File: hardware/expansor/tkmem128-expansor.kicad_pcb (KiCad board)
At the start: 2 copper layers, 78.7 x 45 mm, 3 parts, among them J1 Terminais do conector, J2 Passagem

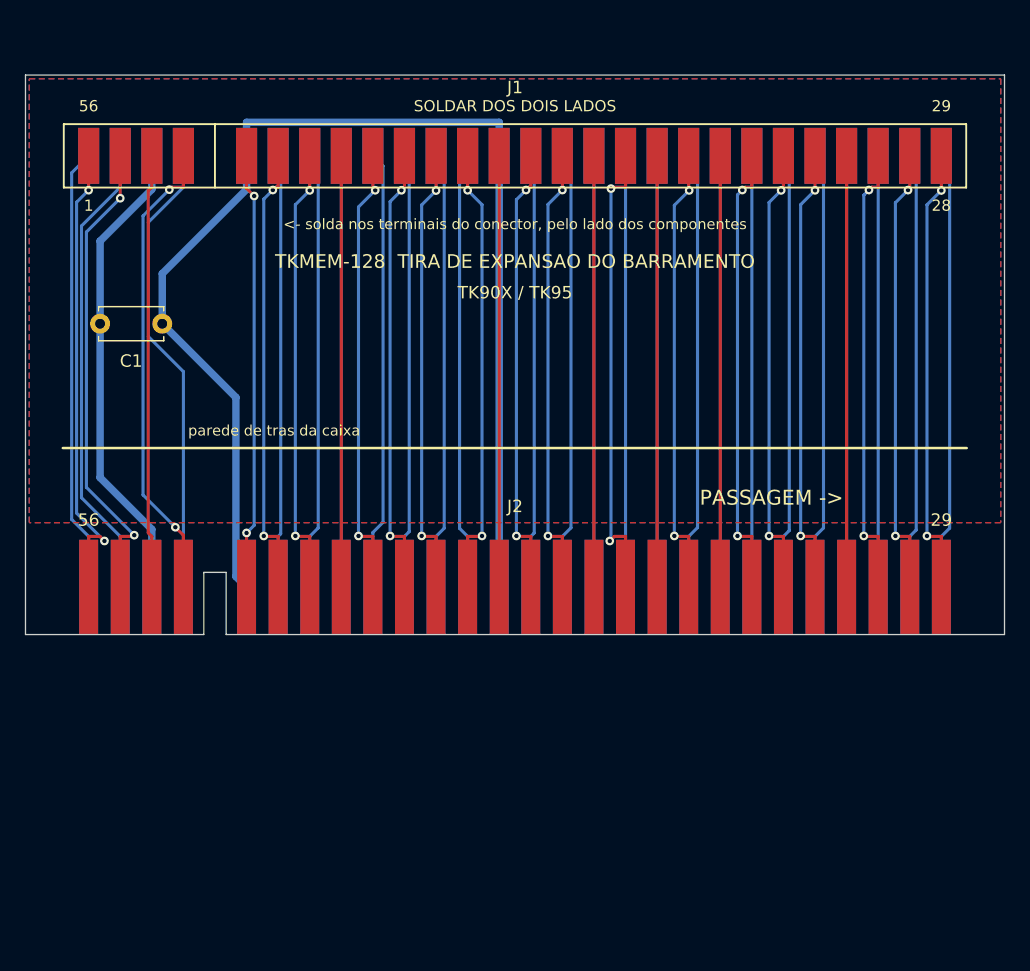
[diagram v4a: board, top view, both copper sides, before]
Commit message: Tira de expansao: ilhas de solda chegam ate a borda
As ilhas de J1 agora comecam na propria aresta da tira e entram 5 mm, em vez
de ficarem recuadas. Os terminais do TE 5645235 avancam 3,18 +-0,51 mm, mas ha
conectores com terminal mais curto - com a ilha na borda o terminal encontra
cobre em qualquer caso, e nao importa quanto a tira entra entre as fileiras.

Ajustes que vieram junto:

  mk_decoy.py  ganhou EDGE_PADS_TOP: a placa-isca nao pode recuar a aresta onde
               o cobre chega de proposito na borda, senao as ilhas ficariam
               fora do contorno e o roteador as trataria como obstaculo.
  .kicad_dru   regra de folga cobre-borda dispensada para J1, como ja havia
               para os dedos de J2.

Nota de fabricacao: o ENIG vale para a tira inteira, nao so para os dedos - as
ilhas de solda tambem chegam a borda.

Tira reroteada: ERC 0, DRC 0 erros, 0 desconexoes. Placa principal inalterada.

Co-Authored-By: Claude Opus 5 <noreply@anthropic.com>
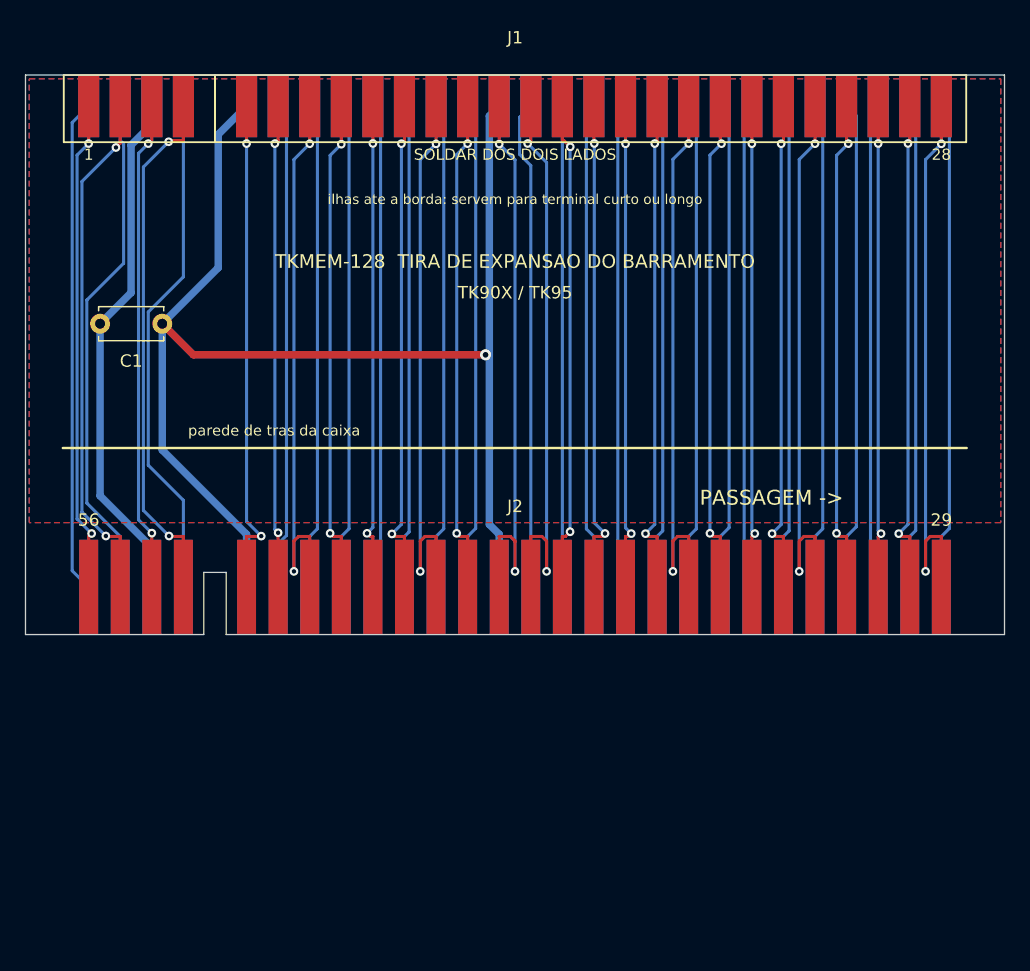
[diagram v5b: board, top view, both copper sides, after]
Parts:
- moved J1 4.00 mm to (39.4, 2.50)
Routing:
- net BUS_NMI: track 34.7 -> 45.9 mm, vias 0 -> 2
- net GND: track 100.7 -> 111.0 mm, vias 0 -> 1
- net BUS_HALT: track 36.3 -> 46.1 mm
- net BUS_P37: track 36.2 -> 45.9 mm
- net D2: track 36.2 -> 45.9 mm
- net BUS_P29: track 36.2 -> 45.9 mm
- net BUS_M1: track 36.2 -> 45.9 mm
- net D4: track 36.2 -> 45.9 mm
- net WR_N: track 34.7 -> 39.9 mm, vias 0 -> 2
- net D6: track 34.7 -> 39.8 mm, vias 0 -> 2
- net BUS_RFSH: track 34.7 -> 39.8 mm, vias 0 -> 2
- net D0: track 35.2 -> 40.3 mm
- net IORQ_N: track 34.7 -> 39.8 mm, vias 0 -> 2
- net BUS_WAIT: track 34.7 -> 39.7 mm, vias 0 -> 2
- net ROMCS_BUS: track 34.7 -> 39.3 mm
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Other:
- board text added: "ilhas ate a borda: servem para terminal curto ou longo"
- board text removed: "<- solda nos terminais do conector, pelo lado dos componentes"

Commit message: Tira estava espelhada em relacao a placa principal
A tira e soldada nos terminais do conector da principal, mas as colunas das
duas estavam invertidas ponta a ponta:

               coluna do pino 1     guia (coluna sem contato)
  principal    x = 73,66 mm         x = 63,50 mm
  tira         x =  5,08 mm         x = 15,24 mm     <- espelhado

Os dois layouts correm no MESMO sentido de X do mundo. Pela regra do KiCad
(Xl x Yl = -N para a face F.Cu vista de fora):

  principal: N = -Y (componentes para tras), Yl = -Z  =>  Xl = +X
  tira:      N = +Z (F.Cu para cima),        Yl = -Y  =>  Xl = +X

Logo a coluna de cada pino e a guia tem que cair no mesmo x nas duas placas.
Corrigido girando J1 e J2 da tira em 180 graus - como todas as ilhas dos dois
footprints estao em y local = 0, girar 180 espelha so o X e nao troca as faces.

Dois reforcos para isso nao voltar:

  gen_pcb.py  o rasgo da guia passa a ser DEDUZIDO do vao real entre as ilhas
              de J2, em vez de calculado pelo numero da coluna. Se o footprint
              girar, o rasgo acompanha.
  tools/confere_alinhamento.py  verificacao de regressao: confere colunas,
              guia, faces das fileiras e qual fileira fica junto a aresta,
              comparando as duas placas. Falha alto se algo desalinhar.

Esse era um erro que ERC e DRC nunca pegariam: cada projeto e valido
isoladamente, nada no KiCad amarra uma placa a outra. So apareceria na bancada,
com o barramento invertido. Documentado no item 5b de ANTES-DE-FABRICAR.

Tira reroteada: ERC 0, DRC 0 erros, 0 desconexoes. Principal inalterada.

Co-Authored-By: Claude Opus 5 <noreply@anthropic.com>
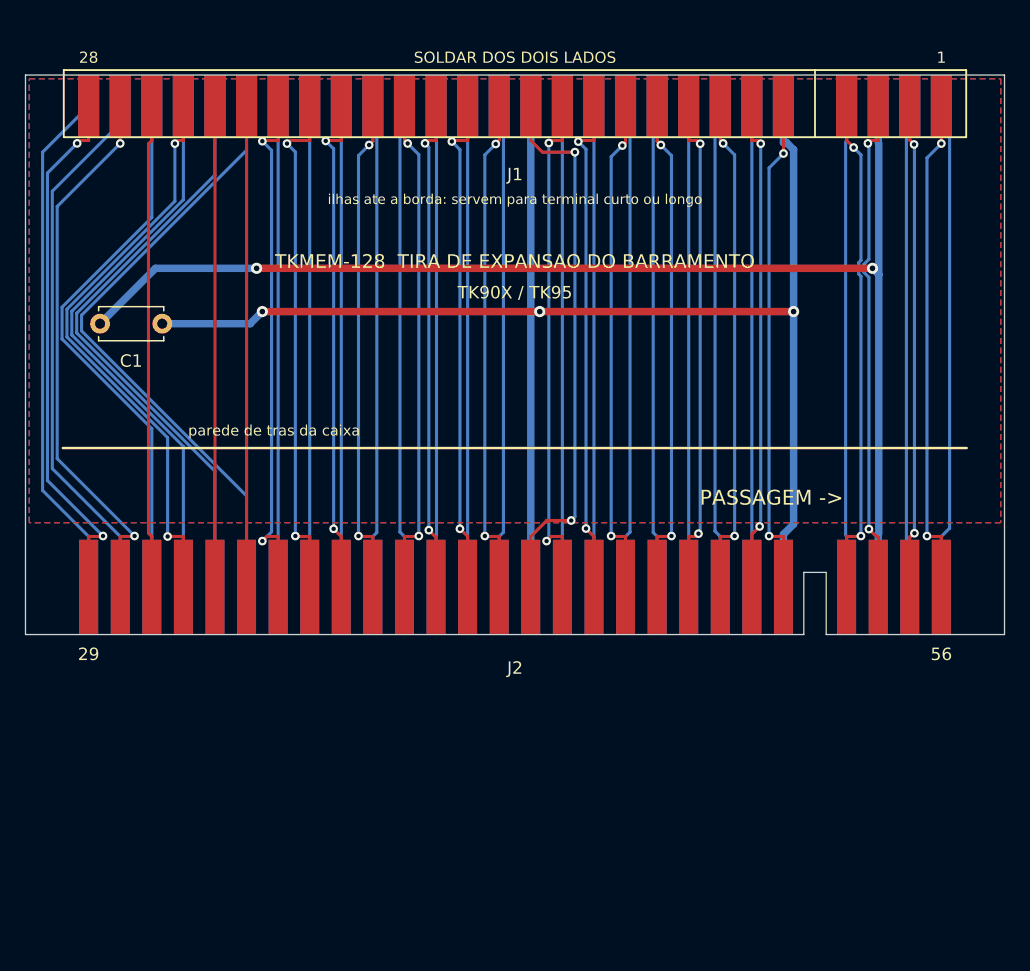
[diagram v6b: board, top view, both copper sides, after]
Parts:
- turned J1 to 180 degrees
- turned J2 to 180 degrees
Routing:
- net +5V: track 42.1 -> 103.3 mm, vias 0 -> 2
- net GND: track 111.0 -> 130.1 mm, vias 1 -> 3
- net A5: track 39.1 -> 49.7 mm
- net A4: track 39.2 -> 47.9 mm
- net BUS_RFSH: track 39.8 -> 47.4 mm
- net BUS_M1: track 45.9 -> 38.7 mm, vias 2 -> 0
- net ROMCS_BUS: track 39.3 -> 46.1 mm
- net BUS_HALT: track 46.1 -> 40.2 mm
- net D2: track 45.9 -> 40.2 mm
- net D4: track 45.9 -> 40.3 mm
- net BUS_P37: track 45.9 -> 40.4 mm
- net BUS_BUSACK: track 39.2 -> 44.7 mm
- net A10: track 39.8 -> 44.4 mm
- net A9: track 39.1 -> 43.2 mm
- net BUS_P35: track 38.9 -> 42.3 mm
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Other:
- outline, holes or cut-outs redrawn

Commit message: Serigrafia da tira: numeracao por face, nas duas faces
As ilhas de J1 e os dedos de J2 sao SMD — cada pino existe em UMA face so. Na
coluna x=73,66 o cobre de F.Cu e o pino 56 e o de B.Cu e o pino 1. A serigrafia
da frente de J1 estava escrita "1" e "28": nomeando os pads de tras. Vira
56 / 29. J2, do lado, ja estava certo, o que so deixava a divergencia mais
visivel na placa.

A tira e soldada dos DOIS lados, entao quem monta olha as duas faces. Cada face
passa a trazer a numeracao dos seus proprios pinos, em J1 e em J2:

  F.Silkscreen   29 ..... 56      (os pads de F.Cu)
  B.Silkscreen    1 ..... 28      (os pads de B.Cu)

Vem trocado de lado entre as faces porque e a mesma placa vista por tras.
"SOLDAR DOS DOIS LADOS" tambem passa a aparecer no verso, que e justamente onde
alguem pode nao perceber que ha o que soldar.

Contorno de J1 refeito: era um retangulo fechado, mas do lado das ilhas fica a
ARESTA da placa, entao um dos lados caia fora da placa e a marca da guia
atravessava a borda (3 avisos de silk_edge_clearance, agora duplicados ao levar
o desenho para o verso). Vira um U aberto para a aresta, parando 0,3 mm antes
dela, nas duas faces. DRC da tira: de 3 avisos para 0.

"PASSAGEM ->" era ambiguo: a flecha apontava para +x, mas os dedos ficam para
baixo. Vira "PARA OUTROS PERIFERICOS", centrado logo acima deles — a
proximidade ja diz a direcao, e o texto diz o que e.

confere_alinhamento.py ganhou a verificacao dessa classe de erro: para cada
rotulo numerico de serigrafia, acha o pad mais proximo NAQUELA face e exige que
o numero bata. Verificado com teste negativo (reintroduzir o erro faz o script
sair com codigo 1). Vale para as duas placas.

Inclui o rearranjo manual do Leonardo no esquematico e na serigrafia das duas
placas.

DRC 0 violacoes, 0 desconexoes. Alinhamento entre as placas inalterado.

Co-Authored-By: Claude Opus 5 <noreply@anthropic.com>
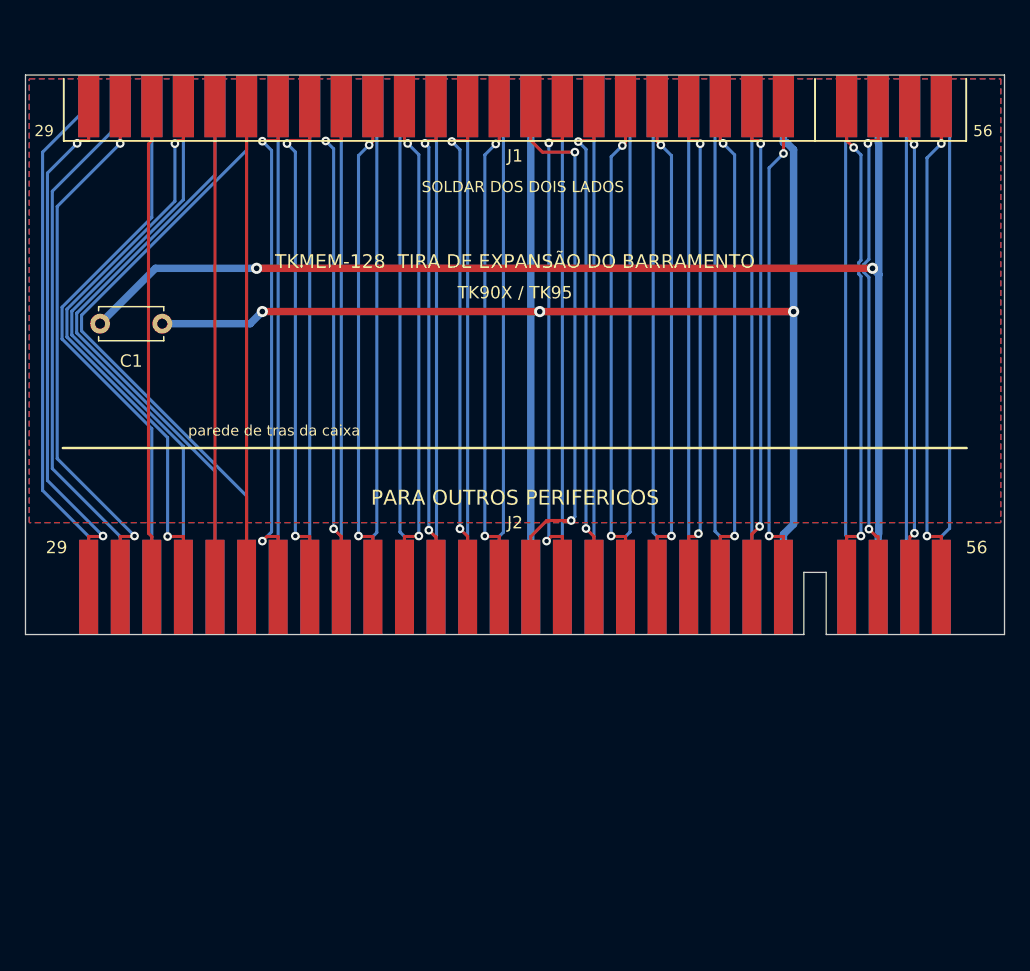
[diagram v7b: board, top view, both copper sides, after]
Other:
- board text added: "Derivado de Velesoft 2009 e Luccas Eletrônica 2012"
- board text added: "PARA OUTROS PERIFERICOS"
- board text added: "TKMEM-128 TIRA DE EXPANSÃO DO BARRAMENTO"
- board text removed: "Derivado de Velesoft 2009 e Luccas Eletronica 2012"
- board text removed: "PASSAGEM ->"
- board text removed: "TKMEM-128 TIRA DE EXPANSAO DO BARRAMENTO"
- board text removed: "ilhas ate a borda: servem para terminal curto ou longo"
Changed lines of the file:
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@@
 		(tags "conector borda edge fingers 56 ZX Spectrum TK90X TK95 passthrough")
 		(property "Reference" "J2"
-			(at 0 -6.5 180)
+			(at 0 5.19 180)
 			(layer "F.SilkS")
 			(effects
@@
 		)
 		(fp_text user "29"
-			(at 34.29 -5.4 180)
+			(at 36.87 3.19 180)
 			(layer "F.SilkS")
 			(effects
@@
 		)
 		(fp_text user "56"
-			(at -34.29 -5.4 180)
+			(at -37.13 3.19 180)
 			(layer "F.SilkS")
 			(effects
@@
 					(thickness 0.15)
 				)
+			)
+		)
+		(fp_text user "28"
+			(at 36.87 3.19 0)
+			(layer "B.SilkS")
+			(effects
+				(font
+					(size 1 1)
+					(thickness 0.15)
+				)
+				(justify mirror)
+			)
+		)
+		(fp_text user "1"
+			(at -37.13 3.19 0)
+			(layer "B.SilkS")
+			(effects
+				(font
+					(size 1 1)
+					(thickness 0.15)
+				)
+				(justify mirror)
 			)
 		)
@@
 		(tags "tira expansao ilhas solda TK90X TK95 barramento")
 		(property "Reference" "J1"
-			(at 0 -5.5 180)
+			(at 0 -4 180)
 			(layer "F.SilkS")
 			(effects
@@
 		(duplicate_pad_numbers_are_jumpers no)
 		(fp_line
+			(start 36.29 -2.8)
+			(end 36.29 2.2)
+			(stroke
+				(width 0.15)
+				(type default)
+			)
+			(layer "F.SilkS")
+		)
+		(fp_line
+			(start 36.29 -2.8)
+			(end -36.29 -2.8)
+			(stroke
+				(width 0.15)
+				(type default)
+			)
+			(layer "F.SilkS")
+		)
+		(fp_line
+			(start -24.13 -2.8)
+			(end -24.13 2.2)
+			(stroke
+				(width 0.15)
+				(type default)
+			)
+			(layer "F.SilkS")
+		)
+		(fp_line
+			(start -36.29 -2.8)
+			(end -36.29 2.2)
+			(stroke
+				(width 0.15)
+				(type default)
+			)
+			(layer "F.SilkS")
+		)
+		(fp_line
+			(start 36.29 -2.8)
+			(end 36.29 2.2)
+			(stroke
+				(width 0.15)
+				(type default)
+			)
+			(layer "B.SilkS")
+		)
+		(fp_line
+			(start 36.29 -2.8)
+			(end -36.29 -2.8)
+			(stroke
+				(width 0.15)
+				(type default)
+			)
+			(layer "B.SilkS")
+		)
+		(fp_line
+			(start -24.13 -2.8)
+			(end -24.13 2.2)
+			(stroke
+				(width 0.15)
+				(type default)
+			)
+			(layer "B.SilkS")
+		)
+		(fp_line
+			(start -36.29 -2.8)
+			(end -36.29 2.2)
+			(stroke
+				(width 0.15)
+				(type default)
+			)
+			(layer "B.SilkS")
+		)
+		(fp_line
 			(start 36.29 2.9)
 			(end -36.29 2.9)
 			(stroke
-				(width 0.15)
-				(type solid)
-			)
-			(layer "F.SilkS")
+				(width 0.05)
+				(type solid)
+			)
+			(layer "F.CrtYd")
 		)
 		(fp_line
@@
 			(end 36.29 2.9)
 			(stroke
-				(width 0.15)
-				(type solid)
-			)
-			(layer "F.SilkS")
-		)
-		(fp_line
-			(start -24.13 -2.5)
-			(end -24.13 2.9)
-			(stroke
-				(width 0.15)
-				(type solid)
-			)
-			(layer "F.SilkS")
+				(width 0.05)
+				(type solid)
+			)
+			(layer "F.CrtYd")
 		)
 		(fp_line
@@
 			(end -36.29 -2.5)
 			(stroke
-				(width 0.15)
-				(type solid)
-			)
-			(layer "F.SilkS")
+				(width 0.05)
+				(type solid)
+			)
+			(layer "F.CrtYd")
 		)
 		(fp_line
@@
 			(end 36.29 -2.5)
 			(stroke
-				(width 0.15)
-				(type solid)
-			)
-			(layer "F.SilkS")
-		)
-		(fp_line
-			(start 36.29 2.9)
-			(end -36.29 2.9)
-			(stroke
 				(width 0.05)
 				(type solid)
@@
 			(layer "F.CrtYd")
 		)
-		(fp_line
-			(start 36.29 -2.5)
-			(end 36.29 2.9)
-			(stroke
-				(width 0.05)
-				(type solid)
-			)
-			(layer "F.CrtYd")
-		)
-		(fp_line
-			(start -36.29 2.9)
-			(end -36.29 -2.5)
-			(stroke
-				(width 0.05)
-				(type solid)
-			)
-			(layer "F.CrtYd")
-		)
-		(fp_line
-			(start -36.29 -2.5)
-			(end 36.29 -2.5)
-			(stroke
-				(width 0.05)
-				(type solid)
-			)
-			(layer "F.CrtYd")
+		(fp_text user "29"
+			(at 37.87 -2 180)
+			(layer "F.SilkS")
+			(effects
+				(font
+					(size 0.9 0.9)
+					(thickness 0.15)
+				)
+			)
+		)
+		(fp_text user "SOLDAR DOS DOIS LADOS"
+			(at -0.63 -6.5 180)
+			(layer "F.SilkS")
+			(effects
+				(font
+					(size 0.9 0.9)
+					(thickness 0.15)
+				)
+			)
+		)
+		(fp_text user "56"
+			(at -37.63 -2 180)
+			(layer "F.SilkS")
+			(effects
+				(font
+					(size 0.9 0.9)
+					(thickness 0.15)
+				)
+			)
 		)
 		(fp_text user "28"
-			(at 34.29 3.9 180)
-			(layer "F.SilkS")
+			(at 37.87 -2 0)
+			(layer "B.SilkS")
 			(effects
 				(font
@@
 					(thickness 0.15)
 				)
+				(justify mirror)
 			)
 		)
 		(fp_text user "SOLDAR DOS DOIS LADOS"
-			(at 0 3.9 180)
-			(layer "F.SilkS")
+			(at -0.63 -6.5 0)
+			(layer "B.SilkS")
 			(effects
 				(font
@@
 					(thickness 0.15)
 				)
+				(justify mirror)
 			)
 		)
 		(fp_text user "1"
-			(at -34.29 3.9 180)
-			(layer "F.SilkS")
+			(at -37.63 -2 0)
+			(layer "B.SilkS")
 			(effects
 				(font
@@
 					(thickness 0.15)
 				)
+				(justify mirror)
 			)
 		)
@@
 		(layer "Edge.Cuts")
 	)
-	(gr_text "ilhas ate a borda: servem para terminal curto ou longo"
-		(at 39.37 10 0)
-		(layer "F.SilkS")
-		(effects
-			(font
-				(size 0.8 0.8)
-				(thickness 0.15)
-			)
-		)
-	)
 	(gr_text "parede de tras da caixa"
 		(at 20 28.6 0)
@@
 		)
 	)
-	(gr_text "TKMEM-128  TIRA DE EXPANSAO DO BARRAMENTO"
+	(gr_text "TKMEM-128  TIRA DE EXPANSÃO DO BARRAMENTO"
 		(at 39.37 15 0)
 		(layer "F.SilkS")
@@
 		)
 	)
-	(gr_text "PASSAGEM ->"
-		(at 60 34 0)
+	(gr_text "PARA OUTROS PERIFERICOS"
+		(at 39.37 34 0)
 		(layer "F.SilkS")
 		(effects
@@
 		)
 	)
-	(gr_text "Derivado de Velesoft 2009 e Luccas Eletronica 2012"
+	(gr_text "Derivado de Velesoft 2009 e Luccas Eletrônica 2012"
 		(at 39.37 25 0)
 		(layer "B.SilkS")
